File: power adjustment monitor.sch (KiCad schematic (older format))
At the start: 0 parts

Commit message: Module 3 Unit 7
Understanding The Power Control, Conditioning And Monitoring Module
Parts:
- added JP? (x3): JUMPER, ~, symbol JUMPER
- added R? (x8): R, ~, symbol R
- added R? (x2): RVAR, ~, symbol RVAR
- added U? (x2): LM317, ~, symbol LM317
- added U? (x2): 7805, ~, symbol 7805
- added U? (x2): LM324, symbol LM324
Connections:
- new net: R?.1, R?.2, U?.2 (ADJ)
- new net: R?.2, R?.2, U?.2 (ADJ)
- new net +12V: JP?.1, U?.1 (IN), U?.4 (V+), U?.4 (V+), U?.VI
- new net -12V: JP?.1, U?.1 (IN), U?.11 (V-), U?.11 (V-), U?.VI
- new net AGND: JP?.1, R?.1, R?.1, R?.1, R?.2, U?.GND, U?.GND
- new net FE_V+: JP?.2, U?.VO
- new net FE_V-: JP?.2, U?.VO
- new net GND: JP?.2
- new net V+ADJ: R?.1, R?.2
- new net V+ADJ_MON: R?.1, R?.2
- new net V+CURRENT_MON: U?.1, U?.2 (-)
- new net V+I_MON: R?.1, R?.2, U?.3 (+), U?.3 (OUT)
- new net V-ADJ: R?.1, R?.1
- new net V-ADJ_MON: R?.1, R?.2
- new net V-CURRENT_MON: U?.1, U?.2 (-)
- new net V-I_MON: R?.2, R?.2, U?.3 (+), U?.3 (OUT)

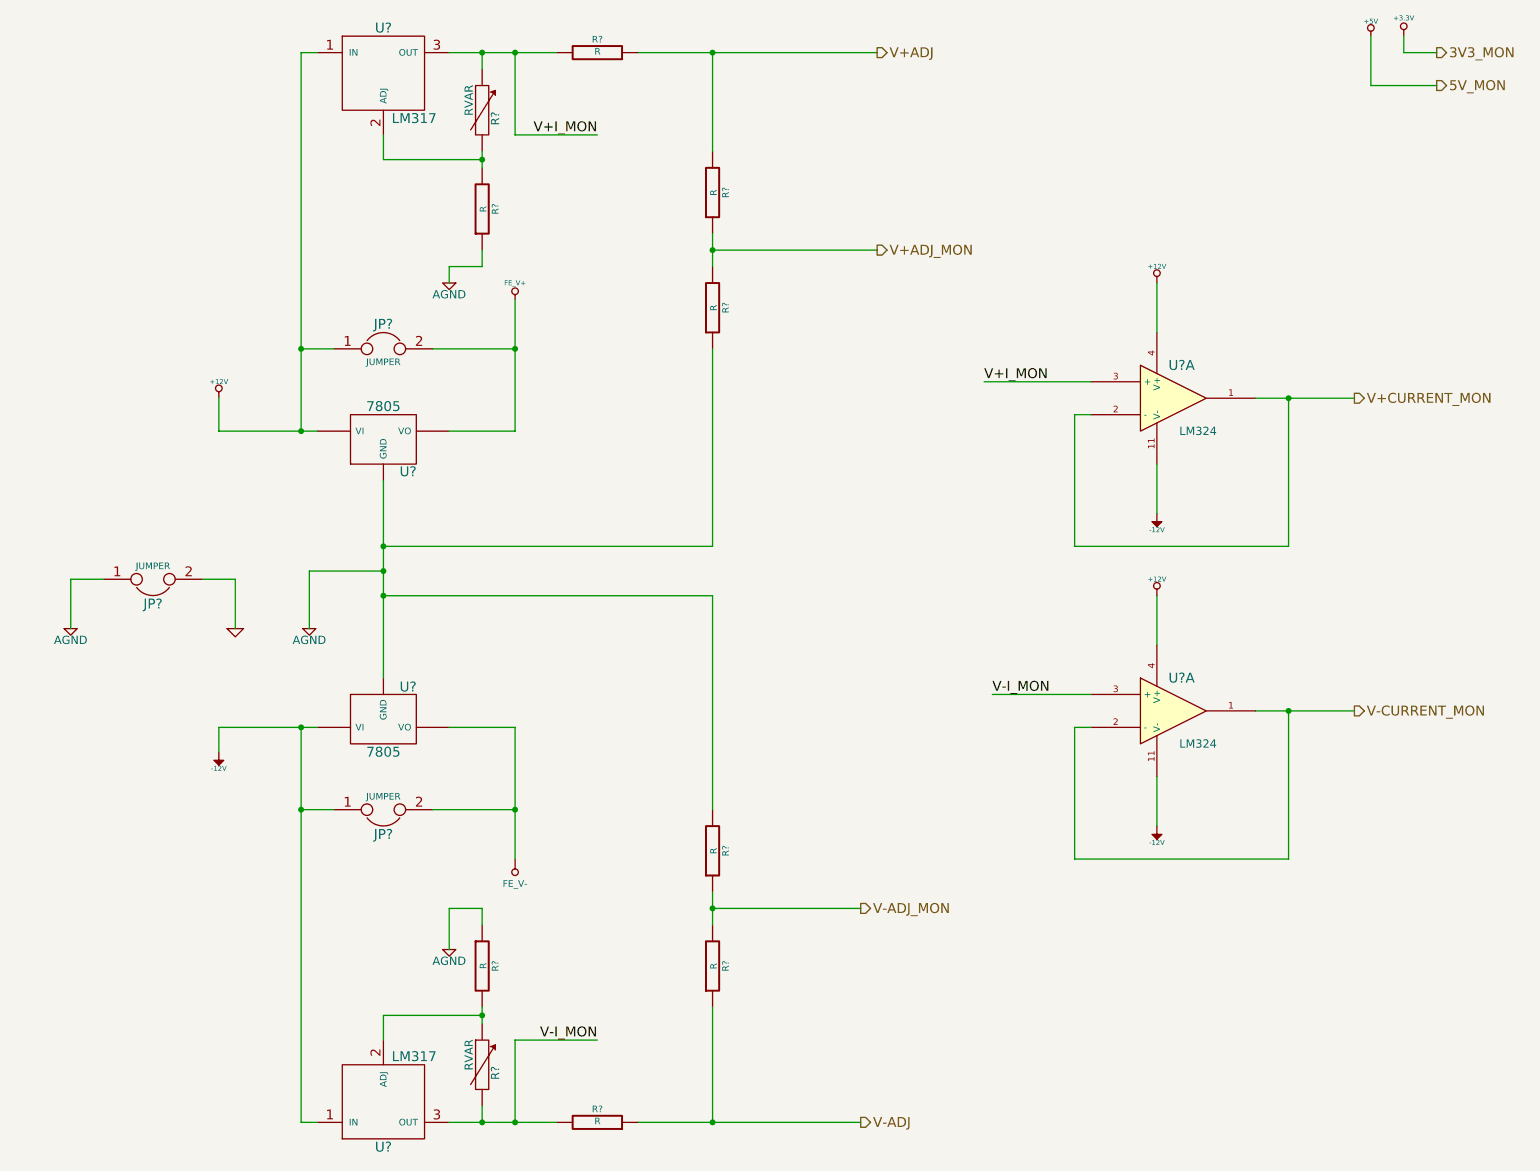
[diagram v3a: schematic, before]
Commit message: Module 3 Unit 15
Choosing Components For The Power Control, Conditioning, Monitoring
Module
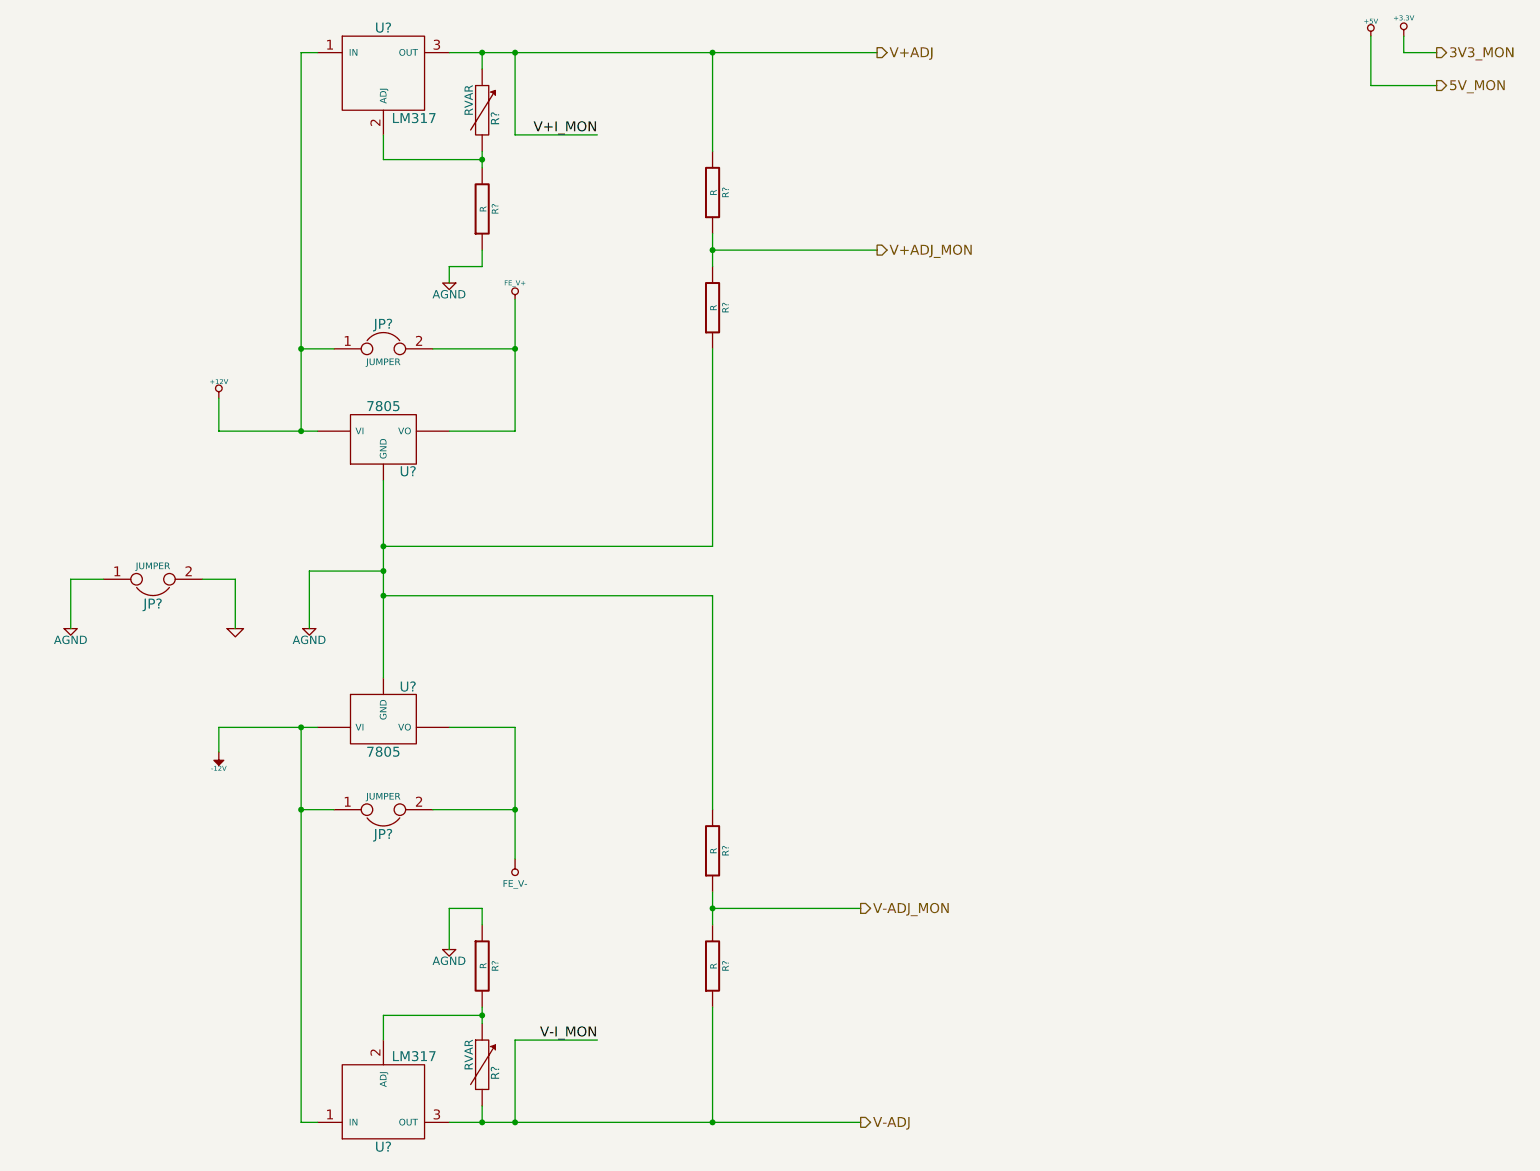
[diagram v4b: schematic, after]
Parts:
- removed R? (x2): R, ~, symbol R
- removed U? (x2): LM324, symbol LM324
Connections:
- net V+I_MON is gone; now on net V+ADJ: R?.1, U?.3 (OUT)
- net V-I_MON is gone; now on net V-ADJ: R?.2, U?.3 (OUT)
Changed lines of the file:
@@
 $Descr A4 11693 8268
 encoding utf-8
-Sheet 9 9
+Sheet 8 9
 Title ""
-Date "16 feb 2014"
+Date "22 feb 2014"
 Rev ""
 Comp ""
@@
 Text HLabel 6500 6200 2    60   Output ~ 0
 V-ADJ_MON
-Text HLabel 9500 3100 2    60   Output ~ 0
-V+CURRENT_MON
-Text HLabel 9500 5000 2    60   Output ~ 0
-V-CURRENT_MON
 $Comp
 L R R?
@@
 	1    0    0    1
 $EndComp
-$Comp
-L R R?
-U 1 1 52FF79D6
-P 4900 1000
-F 0 "R?" V 4980 1000 40  0000 C CNN
-F 1 "R" V 4907 1001 40  0000 C CNN
-F 2 "~" V 4830 1000 30  0000 C CNN
-F 3 "~" H 4900 1000 30  0000 C CNN
-	1    4900 1000
-	0    1    -1   0
-$EndComp
-$Comp
-L R R?
-U 1 1 52FF79DC
-P 4900 7500
-F 0 "R?" V 4980 7500 40  0000 C CNN
-F 1 "R" V 4907 7501 40  0000 C CNN
-F 2 "~" V 4830 7500 30  0000 C CNN
-F 3 "~" H 4900 7500 30  0000 C CNN
-	1    4900 7500
-	0    1    -1   0
-$EndComp
 Text Label 4900 1500 2    60   ~ 0
 V+I_MON
 Text Label 4900 7000 2    60   ~ 0
 V-I_MON
-$Comp
-L LM324 U?
-U 1 1 52FF82BD
-P 8400 3100
-F 0 "U?" H 8450 3300 60  0000 C CNN
-F 1 "LM324" H 8550 2900 50  0000 C CNN
-F 2 "" H 8400 3100 60  0000 C CNN
-F 3 "" H 8400 3100 60  0000 C CNN
-	1    8400 3100
-	1    0    0    -1
-$EndComp
-$Comp
-L -12V #PWR041
-U 1 1 52FF82C6
-P 8300 3800
-F 0 "#PWR041" H 8300 3930 20  0001 C CNN
-F 1 "-12V" H 8300 3900 30  0000 C CNN
-F 2 "" H 8300 3800 60  0000 C CNN
-F 3 "" H 8300 3800 60  0000 C CNN
-	1    8300 3800
-	-1   0    0    1
-$EndComp
-$Comp
-L +12V #PWR042
-U 1 1 52FF82CD
-P 8300 2400
-F 0 "#PWR042" H 8300 2350 20  0001 C CNN
-F 1 "+12V" H 8300 2500 30  0000 C CNN
-F 2 "" H 8300 2400 60  0000 C CNN
-F 3 "" H 8300 2400 60  0000 C CNN
-	1    8300 2400
-	1    0    0    -1
-$EndComp
-$Comp
-L LM324 U?
-U 1 1 52FF82D6
-P 8400 5000
-F 0 "U?" H 8450 5200 60  0000 C CNN
-F 1 "LM324" H 8550 4800 50  0000 C CNN
-F 2 "" H 8400 5000 60  0000 C CNN
-F 3 "" H 8400 5000 60  0000 C CNN
-	1    8400 5000
-	1    0    0    -1
-$EndComp
-$Comp
-L -12V #PWR043
-U 1 1 52FF82DC
-P 8300 5700
-F 0 "#PWR043" H 8300 5830 20  0001 C CNN
-F 1 "-12V" H 8300 5800 30  0000 C CNN
-F 2 "" H 8300 5700 60  0000 C CNN
-F 3 "" H 8300 5700 60  0000 C CNN
-	1    8300 5700
-	-1   0    0    1
-$EndComp
-$Comp
-L +12V #PWR044
-U 1 1 52FF82E3
-P 8300 4300
-F 0 "#PWR044" H 8300 4250 20  0001 C CNN
-F 1 "+12V" H 8300 4400 30  0000 C CNN
-F 2 "" H 8300 4300 60  0000 C CNN
-F 3 "" H 8300 4300 60  0000 C CNN
-	1    8300 4300
-	1    0    0    -1
-$EndComp
 Wire Wire Line
 	2600 3100 2600 3300
@@
 	3100 7500 3200 7500
 Wire Wire Line
-	4000 7500 4650 7500
-Wire Wire Line
-	5150 7500 6500 7500
+	4000 7500 6500 7500
 Wire Wire Line
 	4200 7500 4200 7400
@@
 Connection ~ 5600 7500
 Wire Wire Line
-	4000 1000 4650 1000
-Wire Wire Line
-	5150 1000 6600 1000
+	4000 1000 6600 1000
 Wire Wire Line
 	6600 2200 5600 2200
@@
 	4400 7000 4400 7500
 Connection ~ 4400 7500
-Wire Wire Line
-	8300 3500 8300 3800
-Wire Wire Line
-	8300 2400 8300 2700
-Wire Wire Line
-	8300 5400 8300 5700
-Wire Wire Line
-	8300 4300 8300 4600
-Wire Wire Line
-	8900 3100 9500 3100
-Wire Wire Line
-	8900 5000 9500 5000
-Wire Wire Line
-	7900 3200 7800 3200
-Wire Wire Line
-	7800 3200 7800 4000
-Wire Wire Line
-	7800 4000 9100 4000
-Wire Wire Line
-	9100 4000 9100 3100
-Connection ~ 9100 3100
-Wire Wire Line
-	7900 5100 7800 5100
-Wire Wire Line
-	7800 5100 7800 5900
-Wire Wire Line
-	7800 5900 9100 5900
-Wire Wire Line
-	9100 5900 9100 5000
-Connection ~ 9100 5000
-Text Label 7250 3000 0    60   ~ 0
-V+I_MON
-Text Label 7300 4900 0    60   ~ 0
-V-I_MON
-Wire Wire Line
-	7900 3000 7250 3000
-Wire Wire Line
-	7900 4900 7300 4900
 $Comp
 L RVAR R?
